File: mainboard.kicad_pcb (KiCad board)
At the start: 2 copper layers, 145 parts, among them IC1 ATXMEGA128A1U-A, J1 USB, K1 X_MIN, K2 X_MAX, K3 Y_MIN, K4 Y_MAX, K5 Z_MIN, K6 Z_MAX, P1 POWER, P10 USART, P11 TH_HB, P12 TH_EX, P13 TH_HO, P14 LCD, P15 STP_Y, P16 STP_E0, P17 STP_X, P18 STP_E1, P19 STP_Z, P2 PDI, P20 EXTR, P21 HIC_0, P22 HEATBED, P23 HIC_1, P24 FAN_0, P25 FAN_1, P26 LOC_0, P27 LOC_1, P28 INTERFACE, P3 GPIO_B, P4 BEEPER, P5 OPEN_COLL_D, P6 12V, P7 5V, P8 3.3V, P9 I2C, Q1 IRL1404, Q2 IRL1404, Q3 IRL1404, Q4 IRL1404, SW1 Y, SW2 E0, SW3 X, SW4 E1, SW5 Z, U1 NE 4558 D SMD, U10 ULN_2003_A, U2 ULN_2003_A, U3 A4988-BO, U4 A4988-BO, U5 A4988-BO, U6 A4988-BO, U7 A4988-BO, U8 MCP14E10, U9 MCP14E10

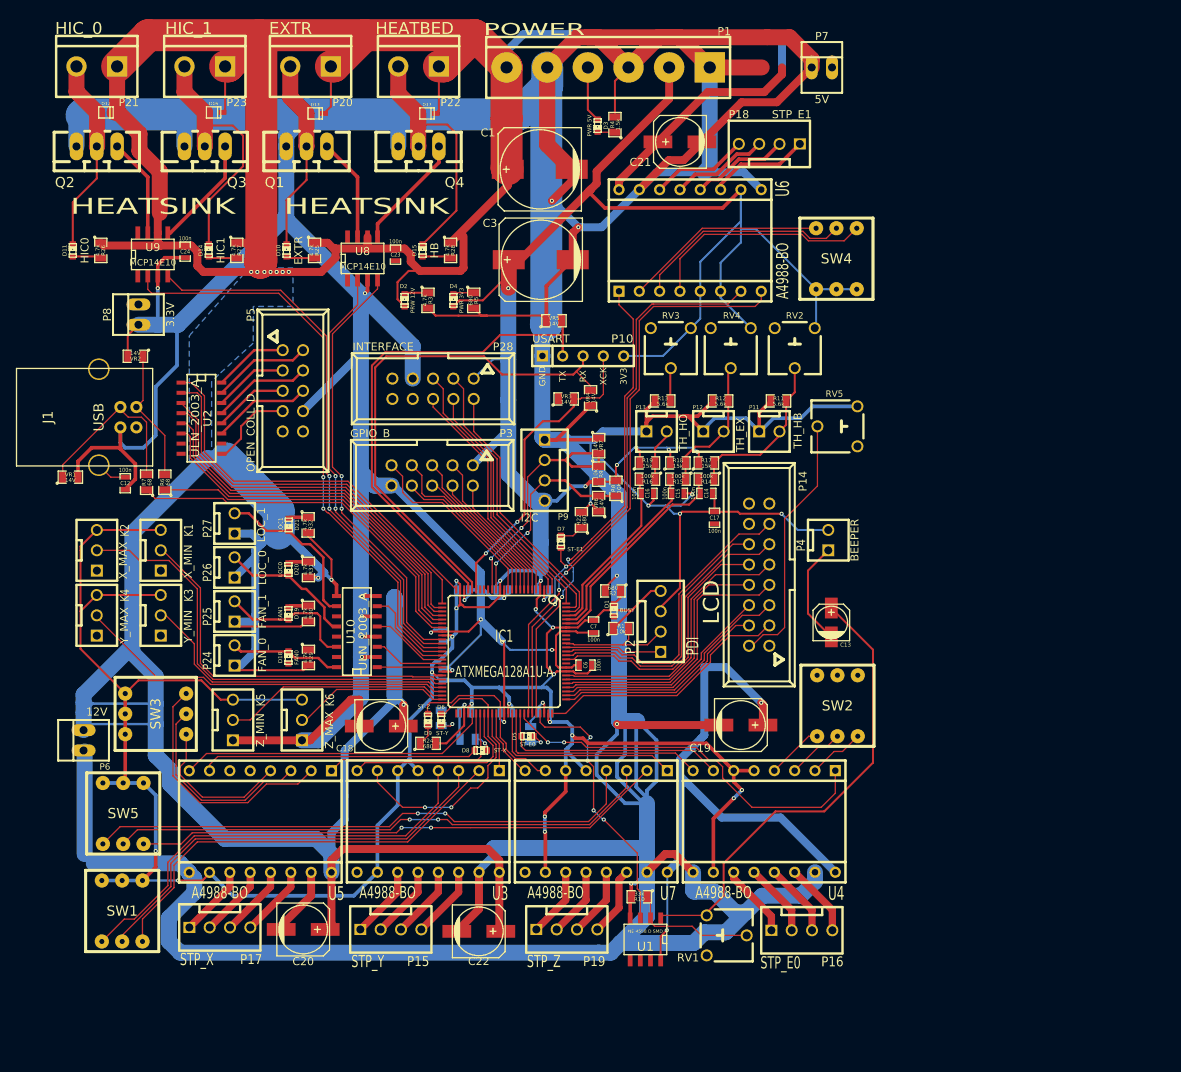
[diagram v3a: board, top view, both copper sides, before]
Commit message: Added board outline
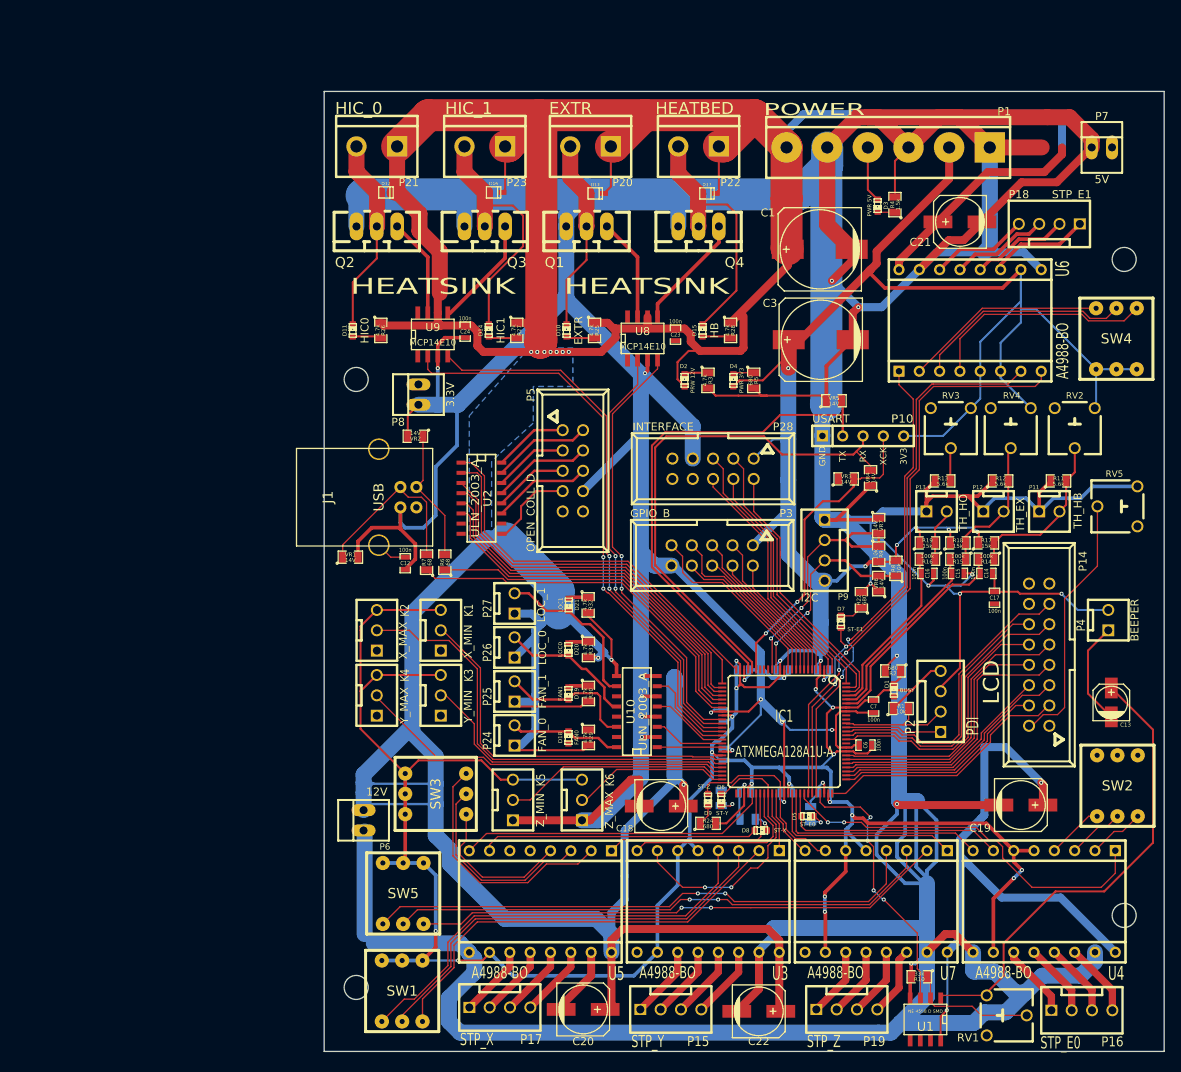
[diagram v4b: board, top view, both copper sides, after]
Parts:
- added ?: MountingHole_3mm_RevA_Date21Jun2010, Mounting_Holes:MountingHole_3mm, F.Cu at (53.0, 57.0)
- added ?: MountingHole_3mm_RevA_Date21Jun2010, Mounting_Holes:MountingHole_3mm, F.Cu at (149.0, 42.0)
- added ?: MountingHole_3mm_RevA_Date21Jun2010, Mounting_Holes:MountingHole_3mm, F.Cu at (149.0, 124.0)
- added ?: MountingHole_3mm_RevA_Date21Jun2010, Mounting_Holes:MountingHole_3mm, F.Cu at (53.0, 133.0)
- moved C13 36.4 mm to (147.4, 97.4)
- moved C19 36.4 mm to (136.1, 110.2)
- moved C21 36.4 mm to (128.5, 37.3)
- moved P12 36.4 mm to (132.7, 73.5)
- moved P18 36.4 mm to (144.7, 37.6)
- moved P4 36.4 mm to (147.0, 87.1)
- moved P7 36.4 mm to (146.2, 28.0)
- moved RV2 36.4 mm to (142.8, 63.1)
- moved RV5 36.4 mm to (148.2, 72.9)
- moved SW2 36.4 mm to (148.2, 107.8)
- moved C22 36.4 mm to (103.3, 136.0)
- moved C23 36.4 mm to (92.9, 51.4)
- moved D13 36.4 mm to (82.9, 33.7)
- moved D17 36.4 mm to (96.8, 33.7)
- moved D2 36.4 mm to (94.1, 57.1)
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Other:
- board outline added: 105 x 120 mm

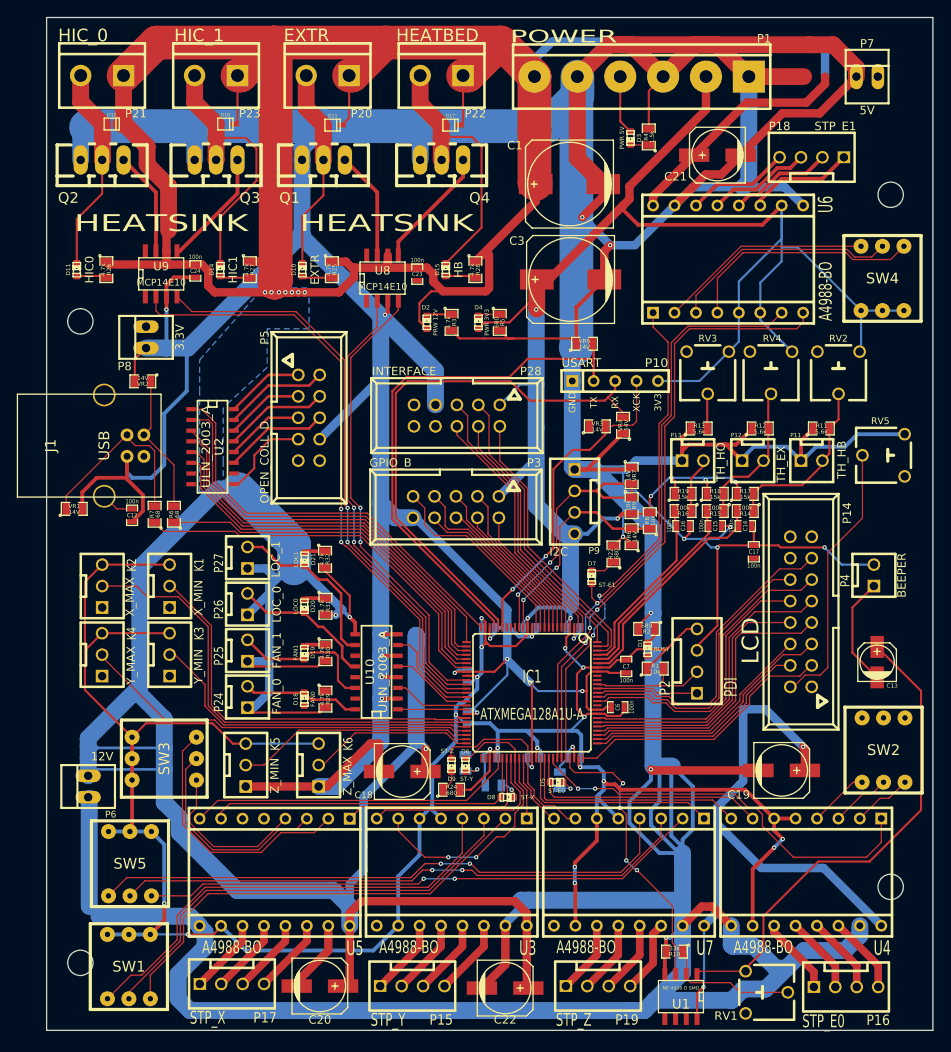
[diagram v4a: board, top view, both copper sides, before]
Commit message: * Added 64Mbit Flash Memory to schematic * Finalized power routing
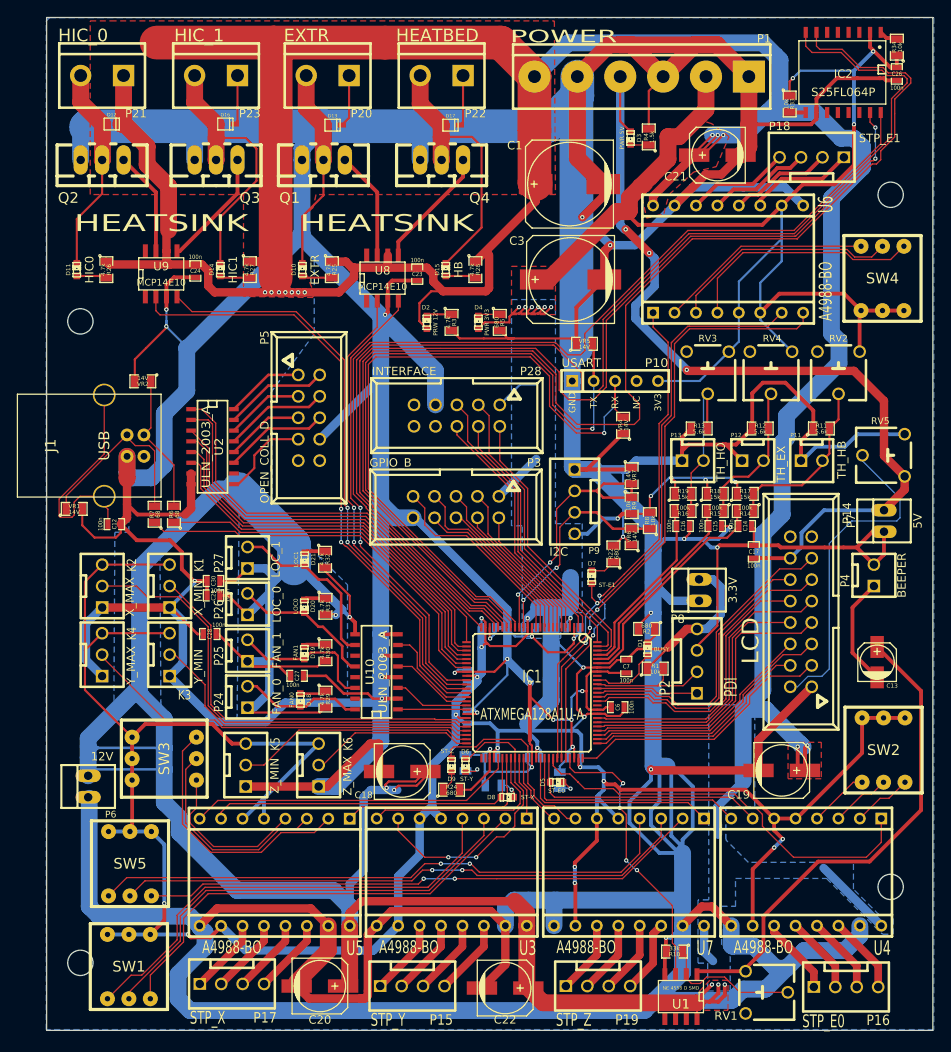
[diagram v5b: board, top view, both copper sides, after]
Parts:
- removed VR3: 14V, SMD_Packages:SM0805
- added C26: 100n, SMD_Packages:SM0603_Capa, F.Cu at (149.7, 27.7)
- added C27: 100n, SMD_Packages:SM0603_Capa, F.Cu at (78.7, 99.0)
- added C28: 100n, SMD_Packages:SM0603_Capa, F.Cu at (68.3, 94.0)
- added C29: 100n, SMD_Packages:SM0603_Capa, F.Cu at (68.8, 89.5)
- added C30: 100n, SMD_Packages:SM0603_Capa, F.Cu at (68.8, 87.8)
- added IC2: S25FL064P, 3dp-special:SO16-Wide, F.Cu at (147.8, 32.3)
- added R33: 10k, SMD_Packages:SM0805, F.Cu at (137.0, 31.2)
- added R34: 10k, SMD_Packages:SM0805, F.Cu at (149.7, 24.5)
- moved P8 72.0 mm to (126.3, 88.8)
- moved P7 52.7 mm to (148.2, 80.6), turned to 90 degrees
- moved C12 2.35 mm to (57.0, 81.0), turned to 0 degrees
- moved D18 0.48 mm to (79.1, 101.9), turned to 270 degrees
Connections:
- IC1 pad 17: Net-(IC1-Pad17) -> /USARTC1-RXD1
- IC1 pad 18: Net-(IC1-Pad18) -> /USARTC1-TXD1
- IC1 pad 19: Net-(IC1-Pad19) -> /FLASH_SPI_CS
- IC1 pad 20: /USARTC1-XCK1 -> /FLASH_SPI_MOSI
- IC1 pad 21: /USARTC1-RXD1 -> /FLASH_SPI_MISO
- IC1 pad 22: /USARTC1-TXD1 -> /FLASH_SPI_SCK
- P10 pad 4: /USARTC1-XCK1 -> Net-(P10-Pad4)
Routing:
- net GND: track 1105.3 -> 1294.6 mm, vias 27 -> 30
- net /FLASH_SPI_CS: track 0.00 -> 155.6 mm
- net /FLASH_SPI_MISO: track 0.00 -> 147.0 mm
- net /FLASH_SPI_MOSI: track 0.00 -> 127.2 mm, vias 0 -> 2
- net /FLASH_SPI_SCK: track 0.00 -> 118.7 mm
- net +5V: track 7.03 -> 105.6 mm, vias 0 -> 3
- net +12V: track 665.2 -> 742.4 mm, vias 12 -> 19
- net +3.3V: track 563.6 -> 640.2 mm, vias 25 -> 32
- net /USARTC1-XCK1: track 39.4 -> 0.00 mm, vias 2 -> 0
- net Net-(C12-Pad1): track 3.92 -> 27.4 mm
- net /USARTC1-RXD1: track 65.0 -> 87.7 mm, vias 0 -> 1
- net /USARTC1-TXD1: track 63.1 -> 82.9 mm, vias 0 -> 1
- net Net-(D1-Pad1): track 0.00 -> 8.13 mm
- net Net-(P13-Pad2): track 10.7 -> 18.8 mm
- net /LCD_CONTR: track 32.2 -> 39.3 mm
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- added copper zone on F.Cu, net +12V
- added copper zone on B.Cu, net +3.3V
- added copper zone on F.Cu, net +3.3V
- added copper zone on B.Cu, net GND

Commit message: * top layer: added filled areas, other optimizations * changed drills, removed bottom solder mask from some through-hole components to make them solderable * added OSHW logo and moved some labels to silkscreen layer * exported gerber files
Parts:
- added G***: LOGO, oshw-logo:oshw-logo-1cm, F.Cu at (68.5, 59.1)
- P10: value USART -> UART
- moved VR1 1.23 mm to (53.4, 79.7), turned to 90 degrees
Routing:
- net GND: track 1294.6 -> 1279.3 mm, vias 30 -> 31
- net Net-(C12-Pad1): track 27.4 -> 25.6 mm
- net /USB+: track 22.5 -> 24.2 mm
- added copper zone on F.Cu, net GND

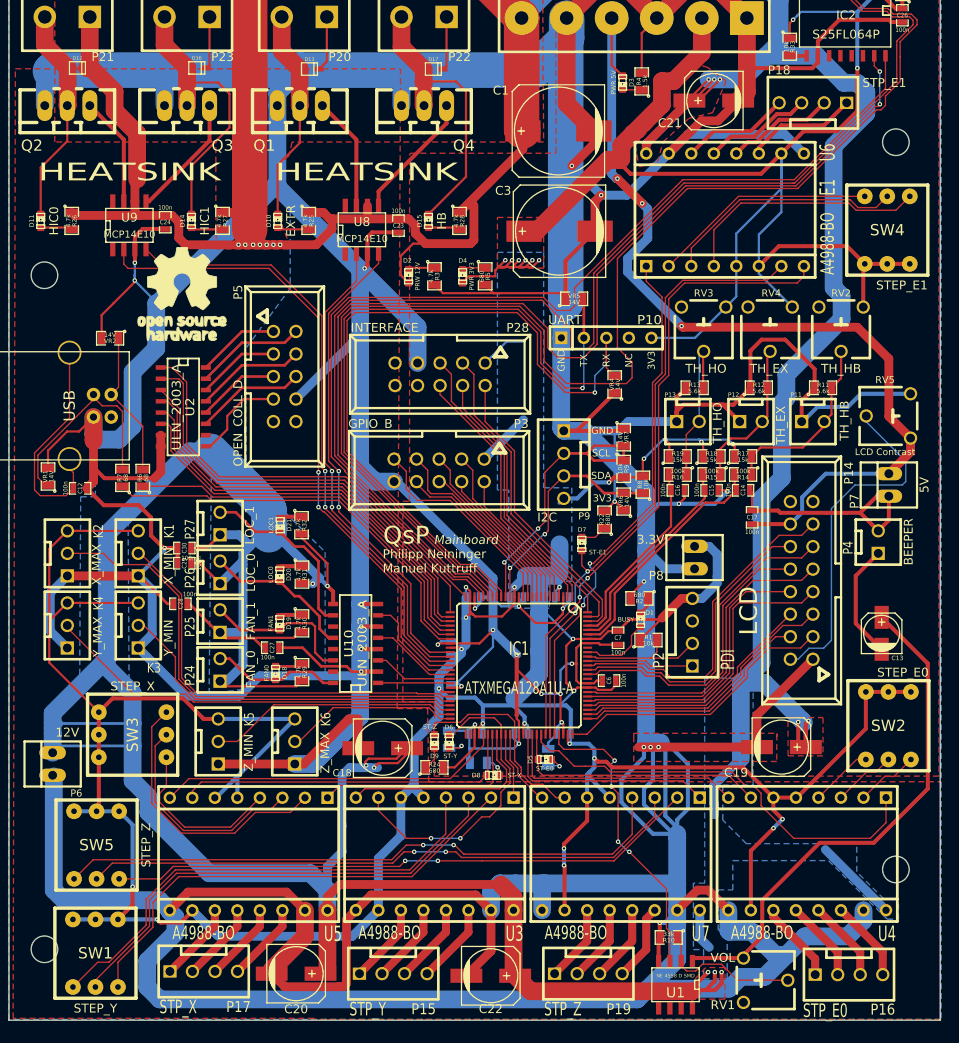
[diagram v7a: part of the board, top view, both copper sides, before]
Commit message: * Added goals for REV B * More room for mounting hole (bottom left)
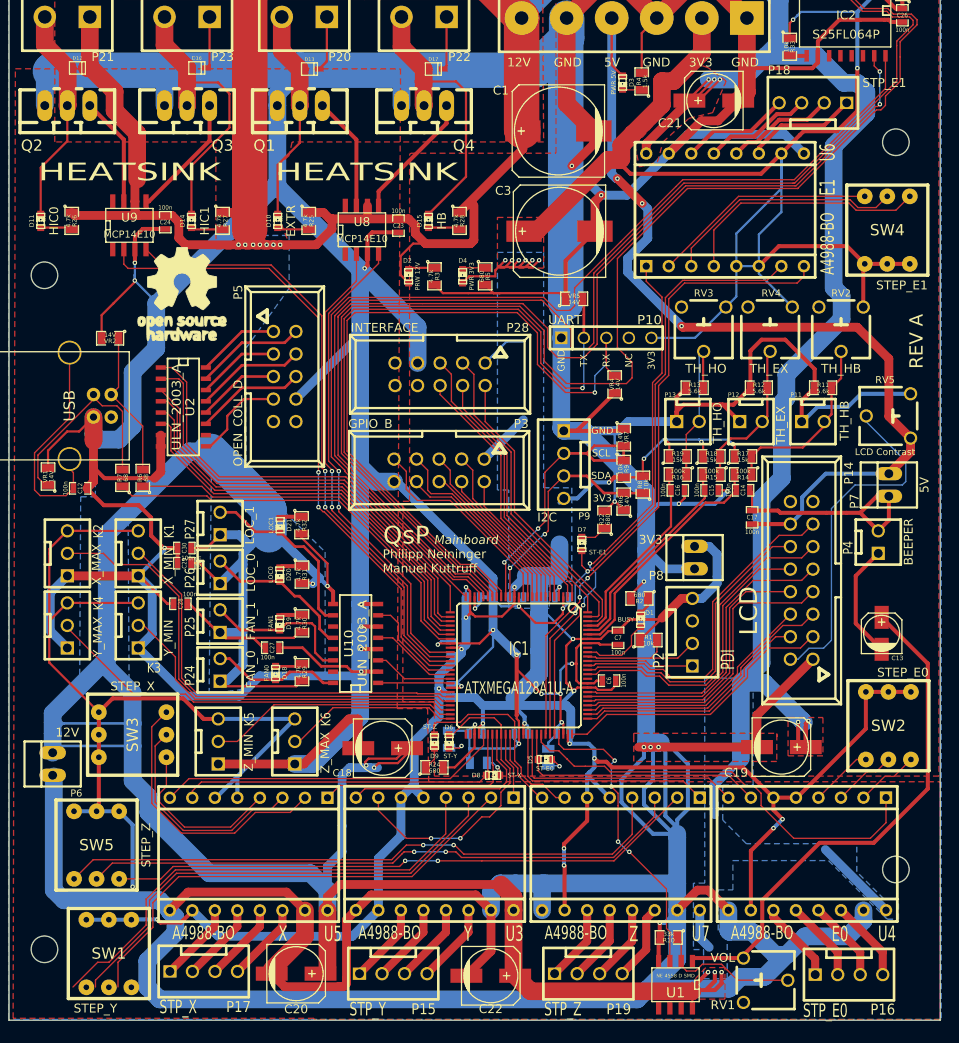
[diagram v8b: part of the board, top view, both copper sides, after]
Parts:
- P8: value 3.3V -> 3V3
- moved SW1 1.51 mm to (60.3, 133.5)
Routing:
- net +3.3V: track 640.0 -> 636.7 mm
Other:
- board text added: "REV A"
